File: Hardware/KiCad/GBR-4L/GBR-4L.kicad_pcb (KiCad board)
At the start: 4 copper layers, 160 x 100 mm, 188 parts, among them J1 USB4105-GF-A, J101 EM7565 M.2 Key B socket, J102 MODEM_CONTROL, J201 EM7565 M.2 Key B socket, J202 MODEM_CONTROL, J301 EM7565 M.2 Key B socket, J302 MODEM_CONTROL, J401 EM7565 M.2 Key B socket, J402 MODEM_CONTROL, J511 2452808-1 nano-SIM, J521 2452808-1 nano-SIM, J531 2452808-1 nano-SIM, J541 2452808-1 nano-SIM, J701 12V INPUT 5A, Q701 30V P-MOSFET low-RDS(on), Q911 MMBT3906, Q921 MMBT3906, Q931 MMBT3906, Q941 MMBT3906, SW911 MODEM 1 RESET, SW912 MODEM 1 RF DISABLE, SW921 MODEM 2 RESET, SW922 MODEM 2 RF DISABLE, SW931 MODEM 3 RESET, SW932 MODEM 3 RF DISABLE, SW941 MODEM 4 RESET, SW942 MODEM 4 RF DISABLE, U1 USBLC6-2SC6, U11 LOW-CAP SIM ESD ARRAY, U12 LOW-CAP SIM ESD ARRAY, U13 LOW-CAP SIM ESD ARRAY, U14 LOW-CAP SIM ESD ARRAY, U2 USB2514Bi-I/M2, U21 TPS56339DDCR, U22 TPS56339DDCR, U23 TPS56339DDCR, U24 TPS56339DDCR, U25 TPS56339DDCR, Y1 24MHz

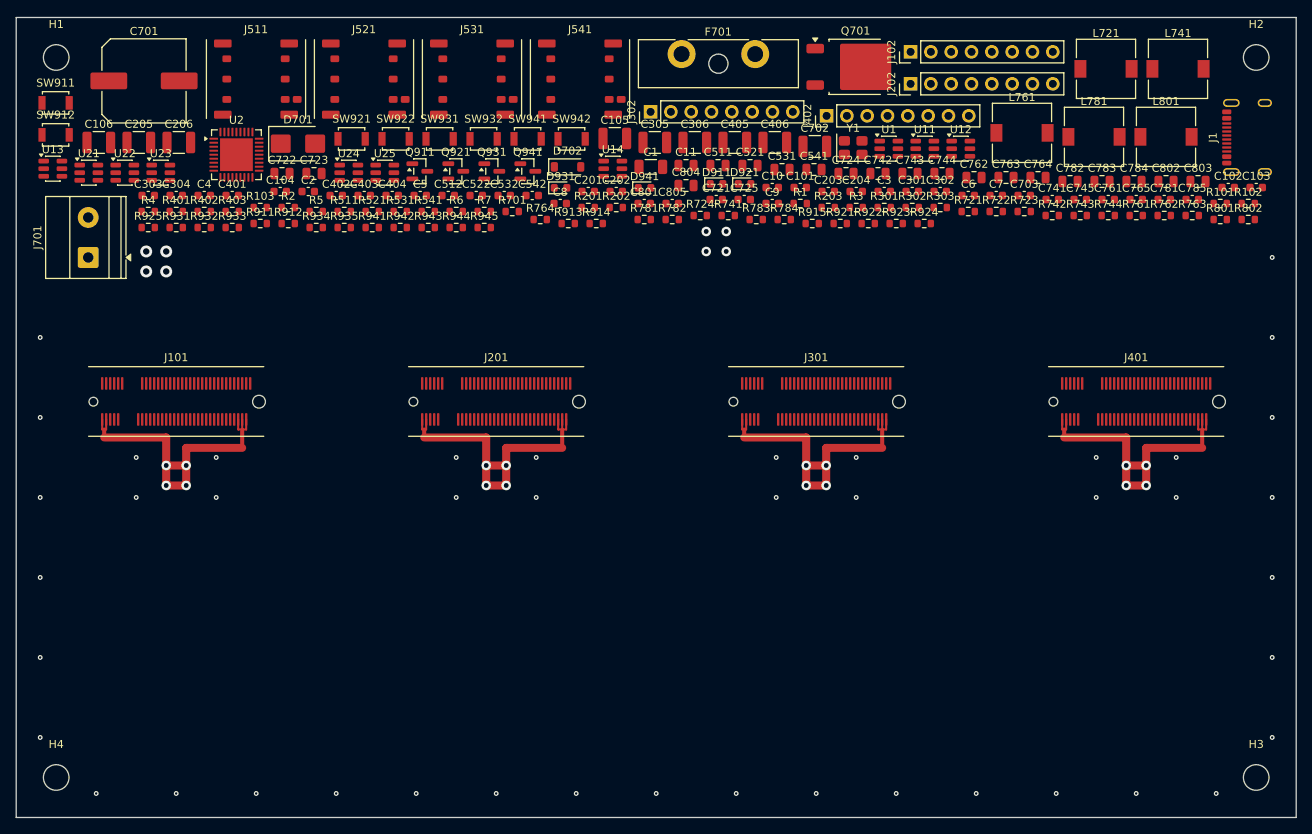
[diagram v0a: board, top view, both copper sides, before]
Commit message: Add stitched outer ground pours
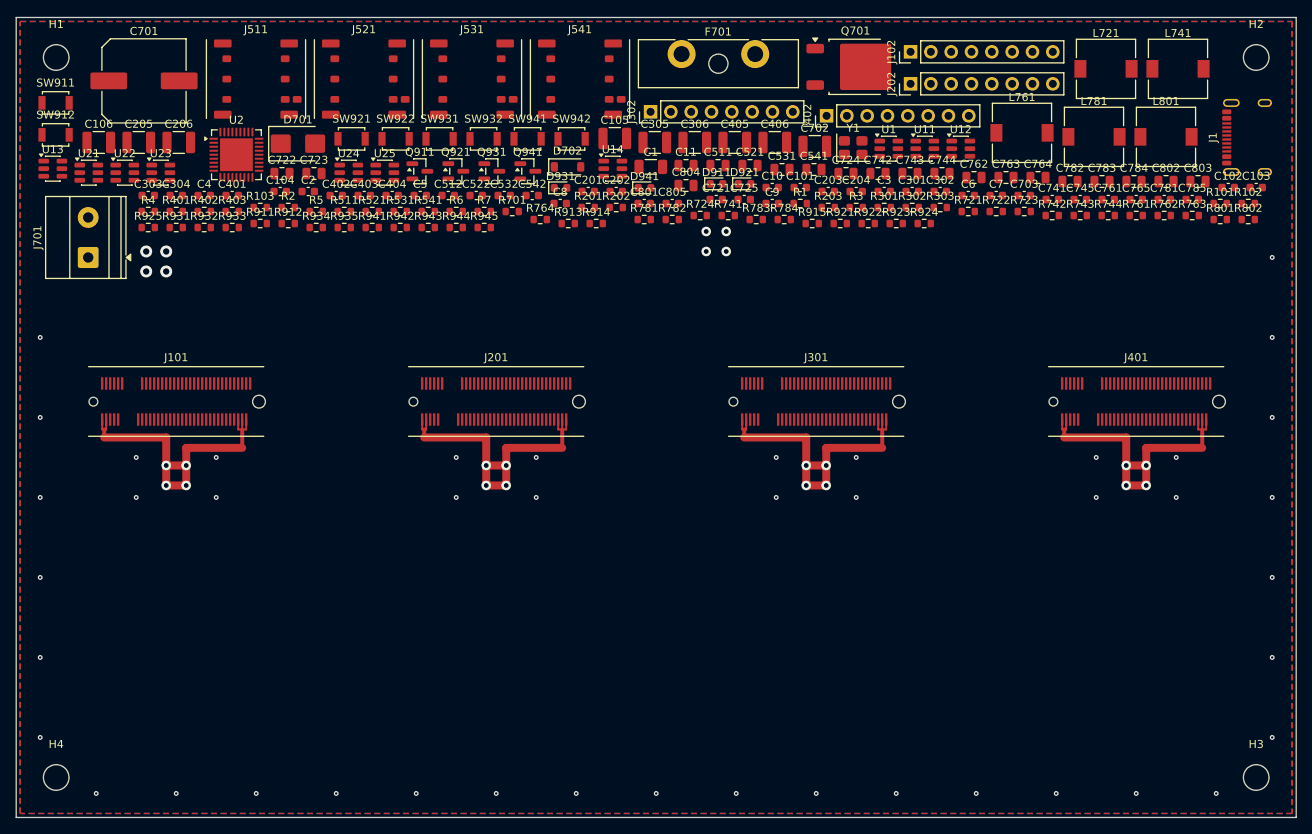
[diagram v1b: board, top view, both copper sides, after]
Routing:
- added copper zone on B.Cu, net GND
- added copper zone on F.Cu, net GND
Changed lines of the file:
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@@
+	(zone
+		(net "GND")
+		(layer "F.Cu")
+		(name "F_OUTER_GND")
+		(hatch edge 0.5)
+		(connect_pads
+			(clearance 0.25)
+		)
+		(min_thickness 0.25)
+		(fill yes
+			(thermal_gap 0.3)
+			(thermal_bridge_width 0.3)
+			(island_removal_mode 2)
+			(island_area_min 5)
+		)
+		(polygon
+			(pts
+				(xy 20.5 20.5) (xy 179.5 20.5) (xy 179.5 119.5) (xy 20.5 119.5)
+			)
+		)
+	)
+	(zone
+		(net "GND")
+		(layer "B.Cu")
+		(name "B_OUTER_GND")
+		(hatch edge 0.5)
+		(connect_pads
+			(clearance 0.25)
+		)
+		(min_thickness 0.25)
+		(fill yes
+			(thermal_gap 0.3)
+			(thermal_bridge_width 0.3)
+			(island_removal_mode 2)
+			(island_area_min 5)
+		)
+		(polygon
+			(pts
+				(xy 20.5 20.5) (xy 179.5 20.5) (xy 179.5 119.5) (xy 20.5 119.5)
+			)
+		)
+	)
 	(zone
 		(net "GND")

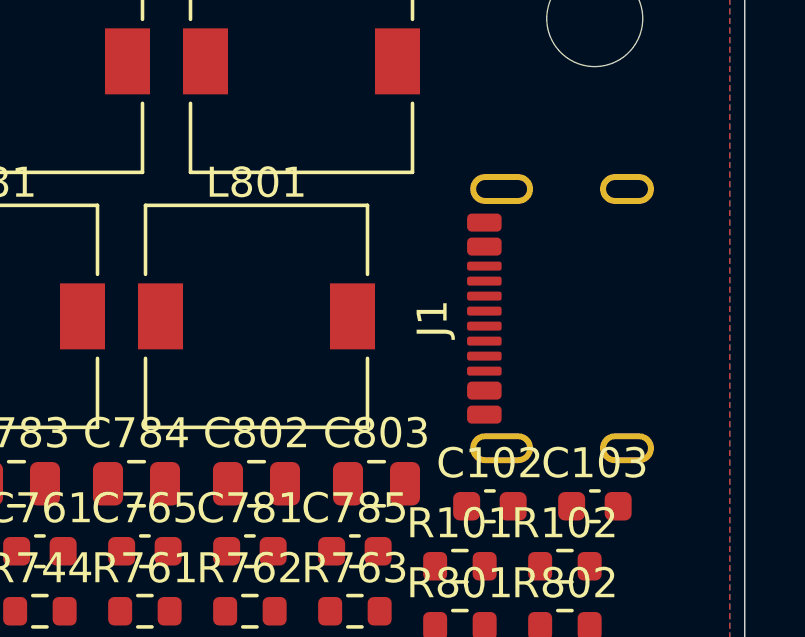
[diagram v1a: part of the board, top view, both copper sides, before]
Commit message: Add USB connector return vias
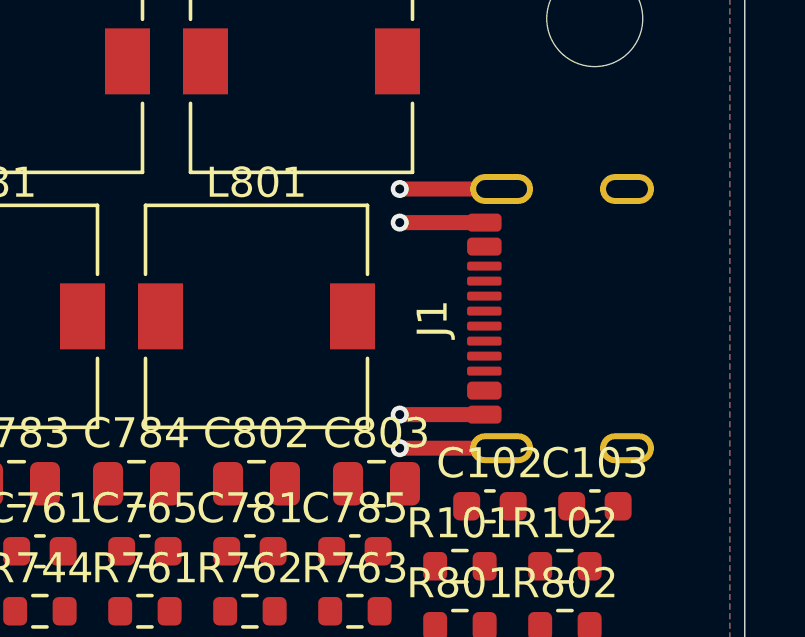
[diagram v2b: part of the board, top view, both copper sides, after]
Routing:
- net USB_SHIELD: track 0.00 -> 6.80 mm, vias 0 -> 2
- net GND: track 0.00 -> 5.64 mm, vias 44 -> 46
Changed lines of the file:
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@@
 		(net "+3V3_M4")
 	)
+	(segment
+		(start 171.32 38.2)
+		(end 168.5 38.2)
+		(width 0.5)
+		(layer "F.Cu")
+		(net "GND")
+	)
+	(segment
+		(start 171.32 31.8)
+		(end 168.5 31.8)
+		(width 0.5)
+		(layer "F.Cu")
+		(net "GND")
+	)
+	(via
+		(at 168.5 31.8)
+		(size 0.6)
+		(drill 0.3)
+		(layers "F.Cu" "B.Cu")
+		(net "GND")
+	)
 	(via
 		(at 60 117)
@@
 	(via
 		(at 23 110)
+		(size 0.6)
+		(drill 0.3)
+		(layers "F.Cu" "B.Cu")
+		(net "GND")
+	)
+	(via
+		(at 168.5 38.2)
 		(size 0.6)
 		(drill 0.3)
@@
 		(net "+3V3_M1")
 	)
+	(segment
+		(start 171.9 39.32)
+		(end 168.5 39.32)
+		(width 0.5)
+		(layer "F.Cu")
+		(net "USB_SHIELD")
+	)
+	(segment
+		(start 171.9 30.68)
+		(end 168.5 30.68)
+		(width 0.5)
+		(layer "F.Cu")
+		(net "USB_SHIELD")
+	)
+	(via
+		(at 168.5 39.32)
+		(size 0.6)
+		(drill 0.3)
+		(layers "F.Cu" "B.Cu")
+		(net "USB_SHIELD")
+	)
+	(via
+		(at 168.5 30.68)
+		(size 0.6)
+		(drill 0.3)
+		(layers "F.Cu" "B.Cu")
+		(net "USB_SHIELD")
+	)
 	(zone

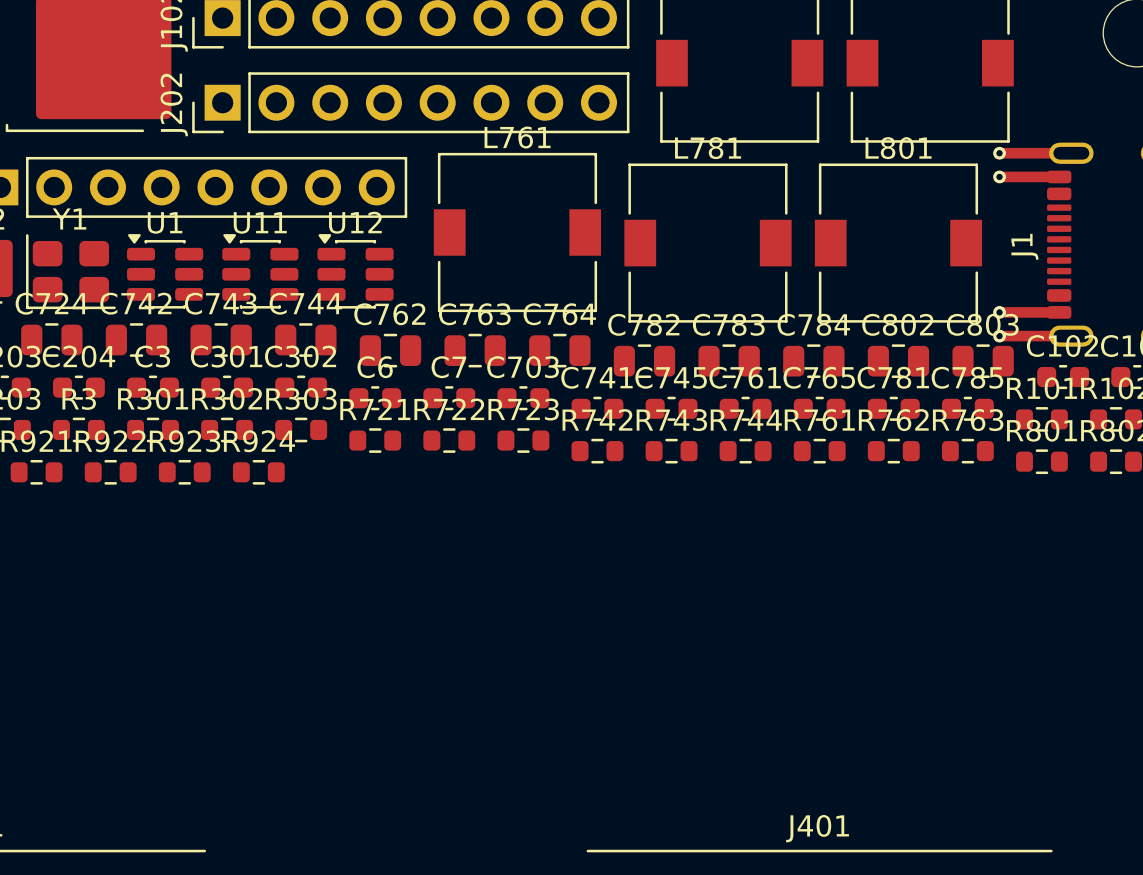
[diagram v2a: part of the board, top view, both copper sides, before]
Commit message: Place USB ESD clamp at connector
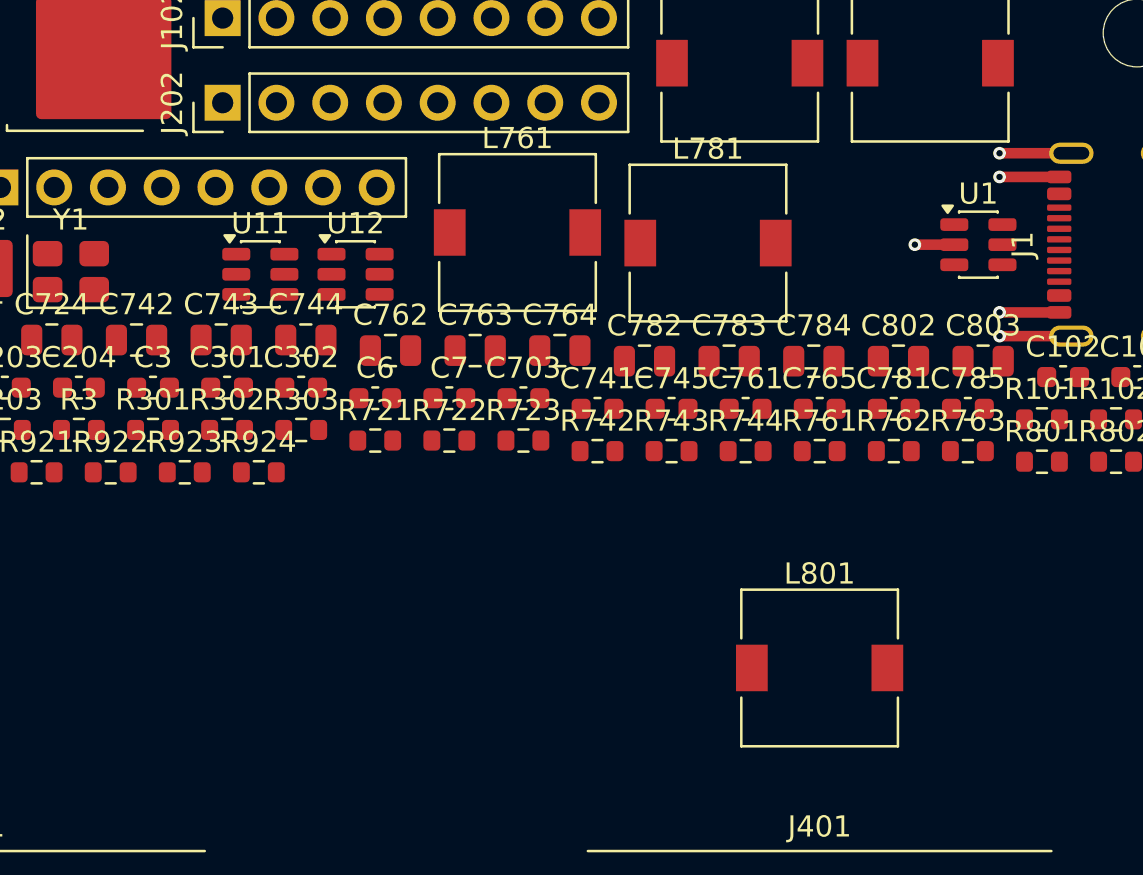
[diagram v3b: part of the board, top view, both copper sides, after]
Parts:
- moved U1 38.5 mm to (167.5, 35.0)
- moved L801 20.4 mm to (160.0, 55.0)
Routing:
- net GND: track 5.64 -> 7.50 mm, vias 46 -> 47
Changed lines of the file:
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@@
 	(footprint "Inductor_SMD:L_7.3x7.3_H3.5"
 		(layer "F.Cu")
-		(at 163.725 34.925)
+		(at 160 55)
 		(descr "Choke, SMD, 7.3x7.3mm 3.5mm height")
 		(tags "Choke SMD")
@@
 	(footprint "Package_TO_SOT_SMD:SOT-23-6"
 		(layer "F.Cu")
-		(at 129.075 36.400001)
+		(at 167.5 35)
 		(descr "SOT, 6 Pin (JEDEC MO-178 Var AB https://www.jedec.org/document_search?search_api_views_fulltext=MO-178)")
 		(tags "SOT TO_SOT_SMD")
@@
 	)
 	(segment
+		(start 166.363 35)
+		(end 164.5 35)
+		(width 0.5)
+		(layer "F.Cu")
+		(net "GND")
+	)
+	(segment
 		(start 171.32 31.8)
 		(end 168.5 31.8)
@@
 		(size 0.6)
 		(drill 0.3)
+		(layers "F.Cu" "B.Cu")
+		(net "GND")
+	)
+	(via
+		(at 164.5 35)
+		(size 0.6)
+		(drill 0.3)

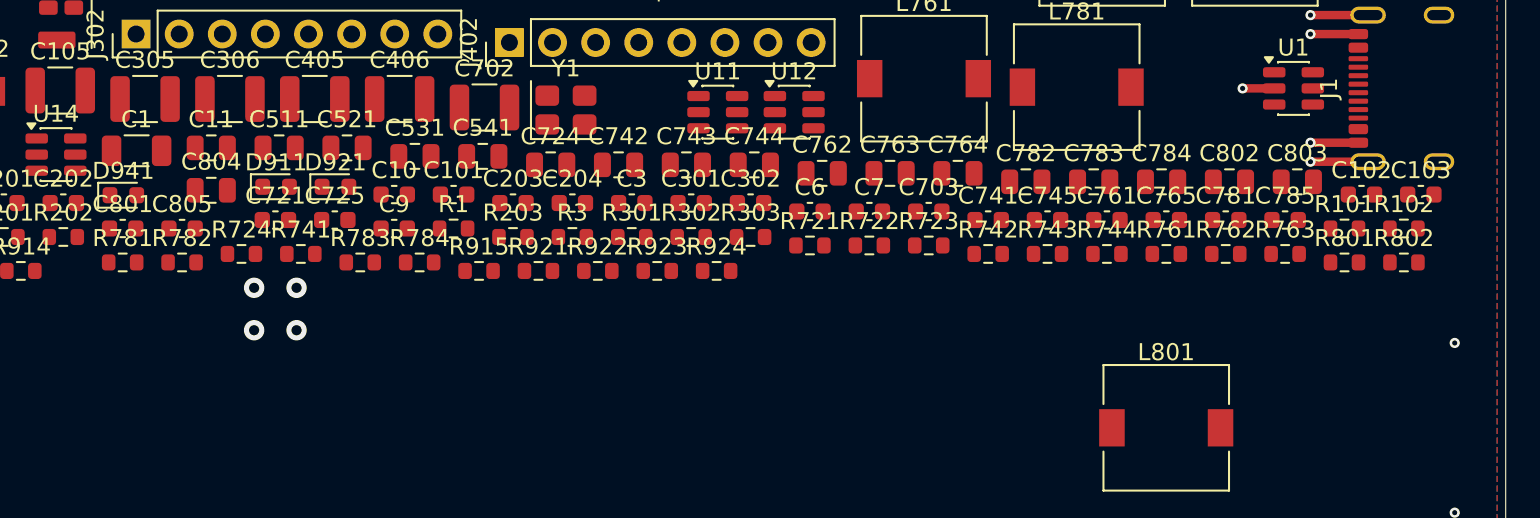
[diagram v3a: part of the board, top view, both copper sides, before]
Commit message: Place USB shield termination network
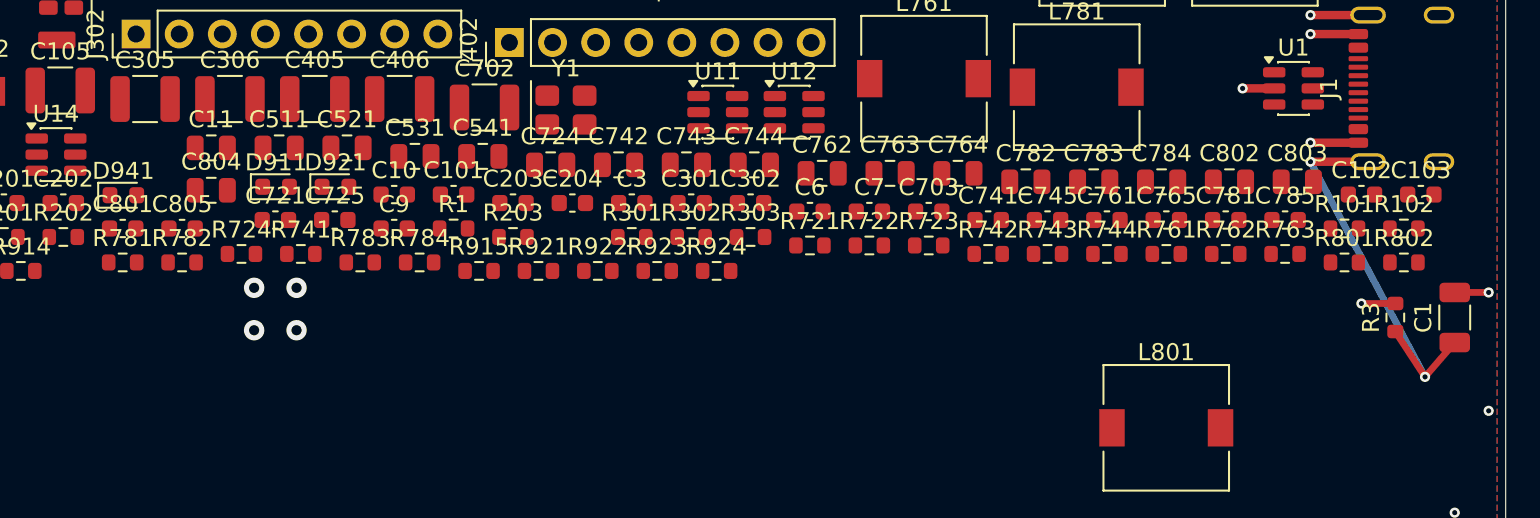
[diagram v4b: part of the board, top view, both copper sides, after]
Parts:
- moved C1 78.3 mm to (177.0, 48.5), turned to 90 degrees
- moved R3 48.7 mm to (173.5, 48.5), turned to 90 degrees
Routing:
- net USB_SHIELD: track 6.80 -> 27.0 mm, vias 2 -> 3
- net GND: track 7.50 -> 11.5 mm, vias 47 -> 49
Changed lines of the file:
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@@
 	(footprint "Resistor_SMD:R_0603_1608Metric"
 		(layer "F.Cu")
-		(at 125.005 43.755)
+		(at 173.5 48.5 90)
 		(descr "Resistor SMD 0603 (1608 Metric), square (rectangular) end terminal, IPC-7351 nominal, (Body size source: IPC-SM-782 page 72, https://www.pcb-3d.com/wordpress/wp-content/uploads/ipc-sm-782a_amendment_1_and_2.pdf)")
 		(tags "resistor")
 		(property "Reference" "R3"
-			(at 0 -1.43 0)
+			(at 0 -1.43 90)
 			(layer "F.SilkS")
 			(effects
@@
 		)
 		(property "Value" "1M"
-			(at 0 1.43 0)
+			(at 0 1.43 90)
 			(layer "F.Fab")
 			(effects
@@
 		)
 		(property "Datasheet" ""
-			(at 0 0 0)
+			(at 0 0 90)
 			(layer "F.Fab")
 			(hide yes)
@@
 		)
 		(property "Description" ""
-			(at 0 0 0)
+			(at 0 0 90)
 			(layer "F.Fab")
 			(hide yes)
@@
 		)
 		(property "KiLib_Generator" "SMD_2terminal_chip_molded"
-			(at 0 0 0)
+			(at 0 0 90)
 			(layer "F.SilkS")
 			(hide yes)
@@
 		)
 		(fp_text user "${REFERENCE}"
-			(at 0 0 0)
+			(at 0 0 90)
 			(layer "F.Fab")
 			(effects
@@
 		)
 		(pad "1" smd roundrect
-			(at -0.825 0)
+			(at -0.825 0 90)
 			(size 0.8 0.95)
 			(layers "F.Cu" "F.Mask" "F.Paste")
@@
 		)
 		(pad "2" smd roundrect
-			(at 0.825 0)
+			(at 0.825 0 90)
 			(size 0.8 0.95)
 			(layers "F.Cu" "F.Mask" "F.Paste")
@@
 	(footprint "Capacitor_SMD:C_1206_3216Metric"
 		(layer "F.Cu")
-		(at 99.325 38.674999)
+		(at 177 48.5 90)
 		(descr "Capacitor SMD 1206 (3216 Metric), square (rectangular) end terminal, IPC-7351 nominal, (Body size source: IPC-SM-782 page 76, https://www.pcb-3d.com/wordpress/wp-content/uploads/ipc-sm-782a_amendment_1_and_2.pdf)")
 		(tags "capacitor")
 		(property "Reference" "C1"
-			(at 0 -1.85 0)
+			(at 0 -1.85 90)
 			(layer "F.SilkS")
 			(effects
@@
 		)
 		(property "Value" "4.7nF 1kV"
-			(at 0 1.85 0)
+			(at 0 1.85 90)
 			(layer "F.Fab")
 			(effects
@@
 		)
 		(property "Datasheet" ""
-			(at 0 0 0)
+			(at 0 0 90)
 			(layer "F.Fab")
 			(hide yes)
@@
 		)
 		(property "Description" ""
-			(at 0 0 0)
+			(at 0 0 90)
 			(layer "F.Fab")
 			(hide yes)
@@
 		)
 		(property "KiLib_Generator" "SMD_2terminal_chip_molded"
-			(at 0 0 0)
+			(at 0 0 90)
 			(layer "F.SilkS")
 			(hide yes)
@@
 		)
 		(fp_text user "${REFERENCE}"
-			(at 0 0 0)
+			(at 0 0 90)
 			(layer "F.Fab")
 			(effects
@@
 		)
 		(pad "1" smd roundrect
-			(at -1.475 0)
+			(at -1.475 0 90)
 			(size 1.15 1.8)
 			(layers "F.Cu" "F.Mask" "F.Paste")
@@
 		)
 		(pad "2" smd roundrect
-			(at 1.475 0)
+			(at 1.475 0 90)
 			(size 1.15 1.8)
 			(layers "F.Cu" "F.Mask" "F.Paste")
@@
 	)
 	(segment
+		(start 177 47.025)
+		(end 179 47.025)
+		(width 0.4)
+		(layer "F.Cu")
+		(net "GND")
+	)
+	(segment
 		(start 166.363 35)
 		(end 164.5 35)
@@
 	)
 	(segment
+		(start 173.5 47.675)
+		(end 171.5 47.675)
+		(width 0.4)
+		(layer "F.Cu")
+		(net "GND")
+	)
+	(segment
 		(start 171.32 31.8)
 		(end 168.5 31.8)
@@
 	)
 	(via
-		(at 177 50)
+		(at 179 54)
 		(size 0.6)
 		(drill 0.3)
@@
 	)
 	(via
+		(at 179 47.025)
+		(size 0.6)
+		(drill 0.3)
+		(layers "F.Cu" "B.Cu")
+		(net "GND")
+	)
+	(via
 		(at 115 80)
 		(size 0.6)
@@
 	)
 	(via
+		(at 171.5 47.675)
+		(size 0.6)
+		(drill 0.3)
+		(layers "F.Cu" "B.Cu")
+		(net "GND")
+	)
+	(via
 		(at 150 117)
 		(size 0.6)
@@
 	)
 	(segment
+		(start 177 49.975)
+		(end 175.25 52)
+		(width 0.4)
+		(layer "F.Cu")
+		(net "USB_SHIELD")
+	)
+	(segment
+		(start 173.5 49.325)
+		(end 175.25 52)
+		(width 0.4)
+		(layer "F.Cu")
+		(net "USB_SHIELD")
+	)
+	(segment
 		(start 171.9 30.68)
 		(end 168.5 30.68)
@@
 		(net "USB_SHIELD")
 	)
+	(via
+		(at 175.25 52)
+		(size 0.6)
+		(drill 0.3)
+		(layers "F.Cu" "B.Cu")
+		(net "USB_SHIELD")
+	)
+	(segment
+		(start 168.5 39.32)
+		(end 175.25 52)
+		(width 0.4)
+		(layer "B.Cu")
+		(net "USB_SHIELD")
+	)

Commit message: Place USB Type-C CC pull-downs
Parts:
- moved R2 119.9 mm to (173.5, 54.0)
- moved R1 52.6 mm to (169.5, 54.0)
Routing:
- net GND: track 11.5 -> 15.5 mm, vias 49 -> 51
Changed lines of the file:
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@@
 	(footprint "Resistor_SMD:R_0603_1608Metric"
 		(layer "F.Cu")
-		(at 54.005 43.754999)
+		(at 173.5 54)
 		(descr "Resistor SMD 0603 (1608 Metric), square (rectangular) end terminal, IPC-7351 nominal, (Body size source: IPC-SM-782 page 72, https://www.pcb-3d.com/wordpress/wp-content/uploads/ipc-sm-782a_amendment_1_and_2.pdf)")
 		(tags "resistor")
@@
 	(footprint "Resistor_SMD:R_0603_1608Metric"
 		(layer "F.Cu")
-		(at 118.004999 43.254999)
+		(at 169.5 54)
 		(descr "Resistor SMD 0603 (1608 Metric), square (rectangular) end terminal, IPC-7351 nominal, (Body size source: IPC-SM-782 page 72, https://www.pcb-3d.com/wordpress/wp-content/uploads/ipc-sm-782a_amendment_1_and_2.pdf)")
 		(tags "resistor")
@@
 	)
 	(segment
+		(start 170.325 54)
+		(end 170.325 56)
+		(width 0.4)
+		(layer "F.Cu")
+		(net "GND")
+	)
+	(segment
 		(start 171.32 31.8)
 		(end 168.5 31.8)
@@
 		(net "GND")
 	)
+	(segment
+		(start 174.325 54)
+		(end 174.325 56)
+		(width 0.4)
+		(layer "F.Cu")
+		(net "GND")
+	)
 	(via
 		(at 168.5 31.8)
@@
 	)
 	(via
+		(at 170.325 56)
+		(size 0.6)
+		(drill 0.3)
+		(layers "F.Cu" "B.Cu")
+		(net "GND")
+	)
+	(via
 		(at 23 80)
 		(size 0.6)
@@
 		(size 0.6)
 		(drill 0.3)
+		(layers "F.Cu" "B.Cu")
+		(net "GND")
+	)
+	(via
+		(at 174.325 56)
+		(size 0.6)
+		(drill 0.3)
